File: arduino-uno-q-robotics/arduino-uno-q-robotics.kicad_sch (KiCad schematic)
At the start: 9 parts, among them J1 Conn_02x30_Odd_Even, J2 Conn_02x30_Odd_Even, J3 Connector_FFC-FPC, J4 Connector_FFC-FPC, U1 LSM6DSO32, U2 TCA9803

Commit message: Add STEMMA port to MCU I2C
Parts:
- added U3: ~, Connector_JST:JST_SH_SM04B-SRSS-TB_1x04-1MP_P1.00mm_Horizontal, symbol robotics-symbols:STEMMA
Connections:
- net +3.3V: now also U3.3 (3.3V)
- net GND: now also U3.4 (GND)
- net MCU_I2C4_SCL: now also U3.1 (SCL)
- net MCU_I2C4_SDA: now also U3.2 (SDA)

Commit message: Adjust STEMMA port pin numbers
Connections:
- net +3.3V: now also U3.2 (3.3V); no longer U3.3 (3.3V)
- net GND: now also U3.1 (GND); no longer U3.4 (GND)
- net MCU_I2C4_SCL: now also U3.4 (SCL); no longer U3.1 (SCL)
- net MCU_I2C4_SDA: now also U3.3 (SDA); no longer U3.2 (SDA)

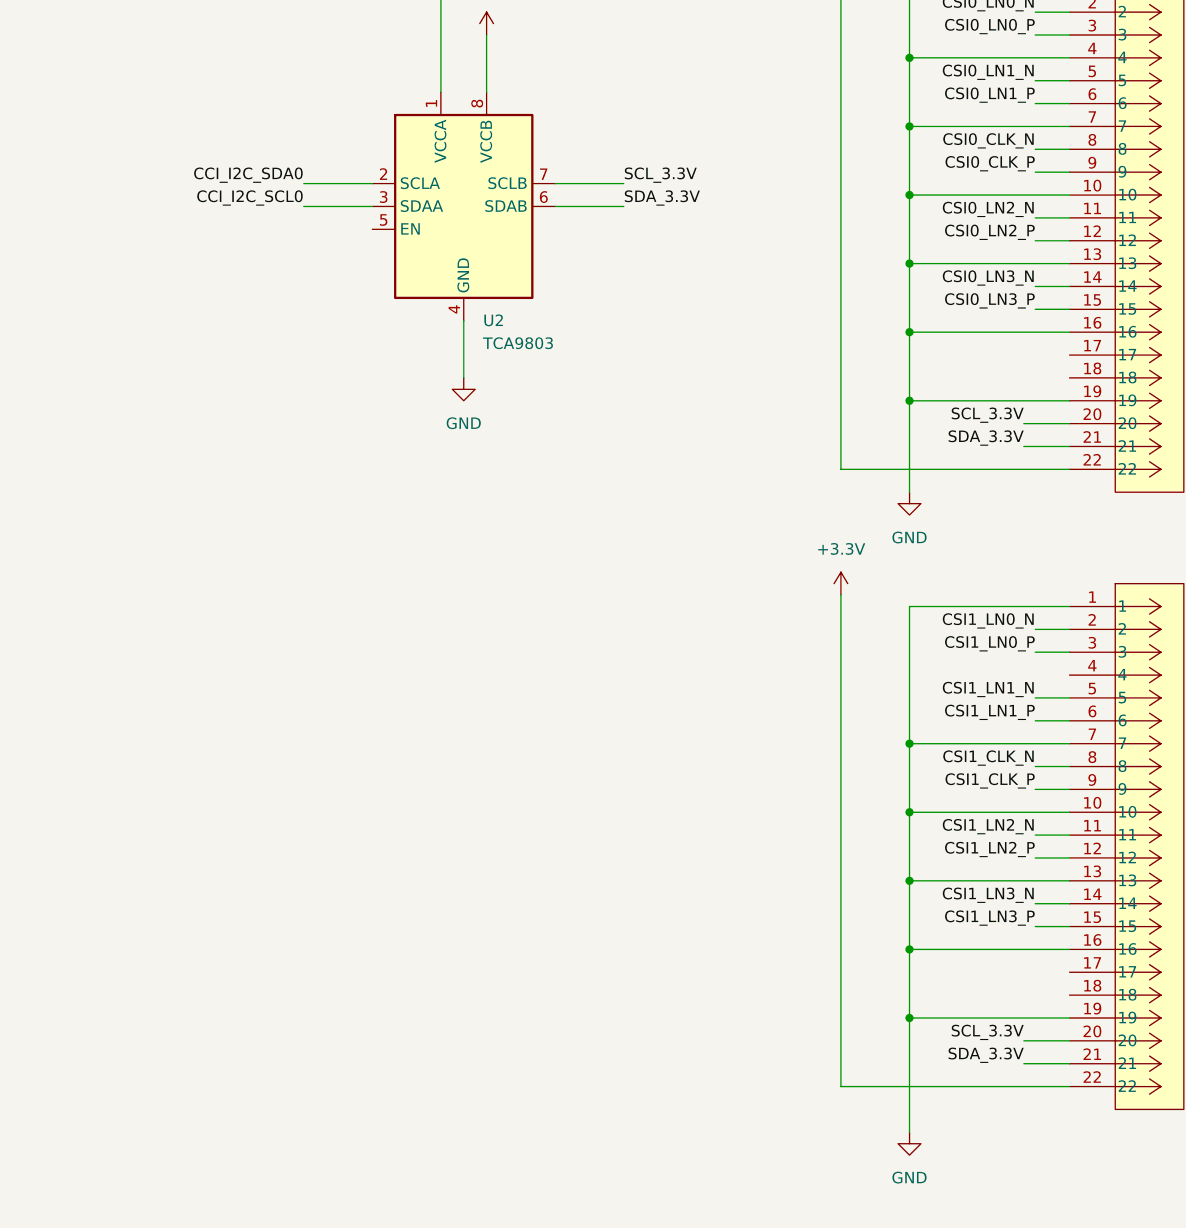
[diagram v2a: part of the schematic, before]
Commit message: Separate camera connectors level shifter
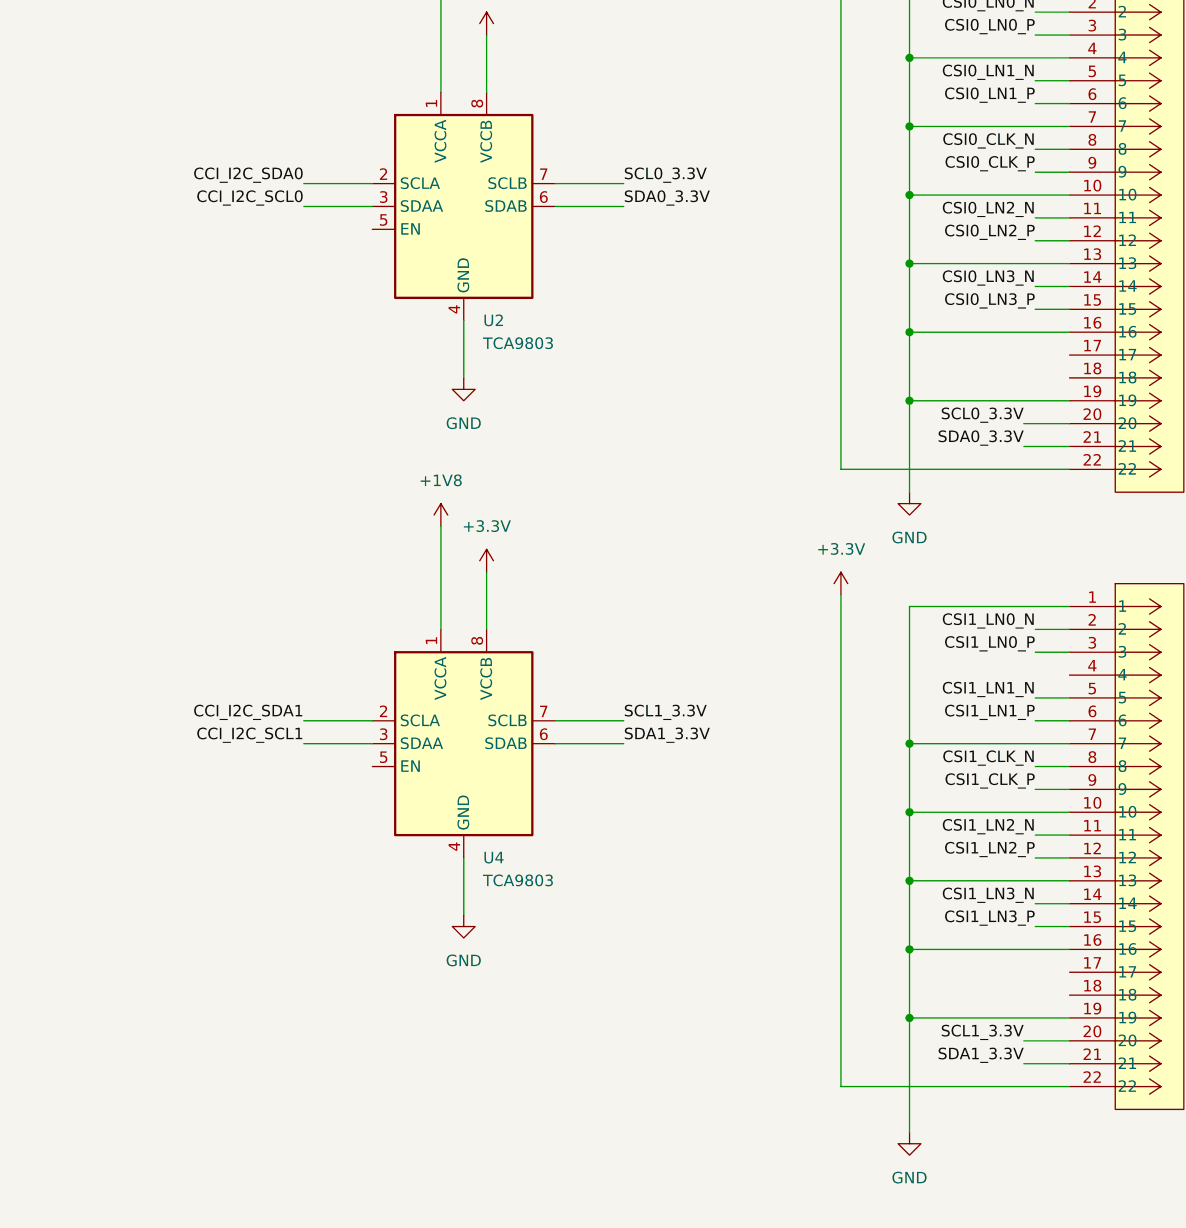
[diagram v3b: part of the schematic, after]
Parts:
- added U4: TCA9803, Package_SO:VSSOP-8_3x3mm_P0.65mm, symbol Interface:TCA9803
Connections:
- net +1V8: now also U4.1 (VCCA)
- net +3.3V: now also U4.8 (VCCB)
- net CCI_I2C_SCL1: now also U4.3 (SDAA)
- net CCI_I2C_SDA1: now also U4.2 (SCLA)
- net GND: now also U4.4 (GND)
- net SCL_3.3V renamed SCL0_3.3V
- net SCL0_3.3V: no longer J4.20
- net SDA_3.3V renamed SDA0_3.3V
- net SDA0_3.3V: no longer J4.21
- new net SCL1_3.3V: J4.20, U4.7 (SCLB)
- new net SDA1_3.3V: J4.21, U4.6 (SDAB)

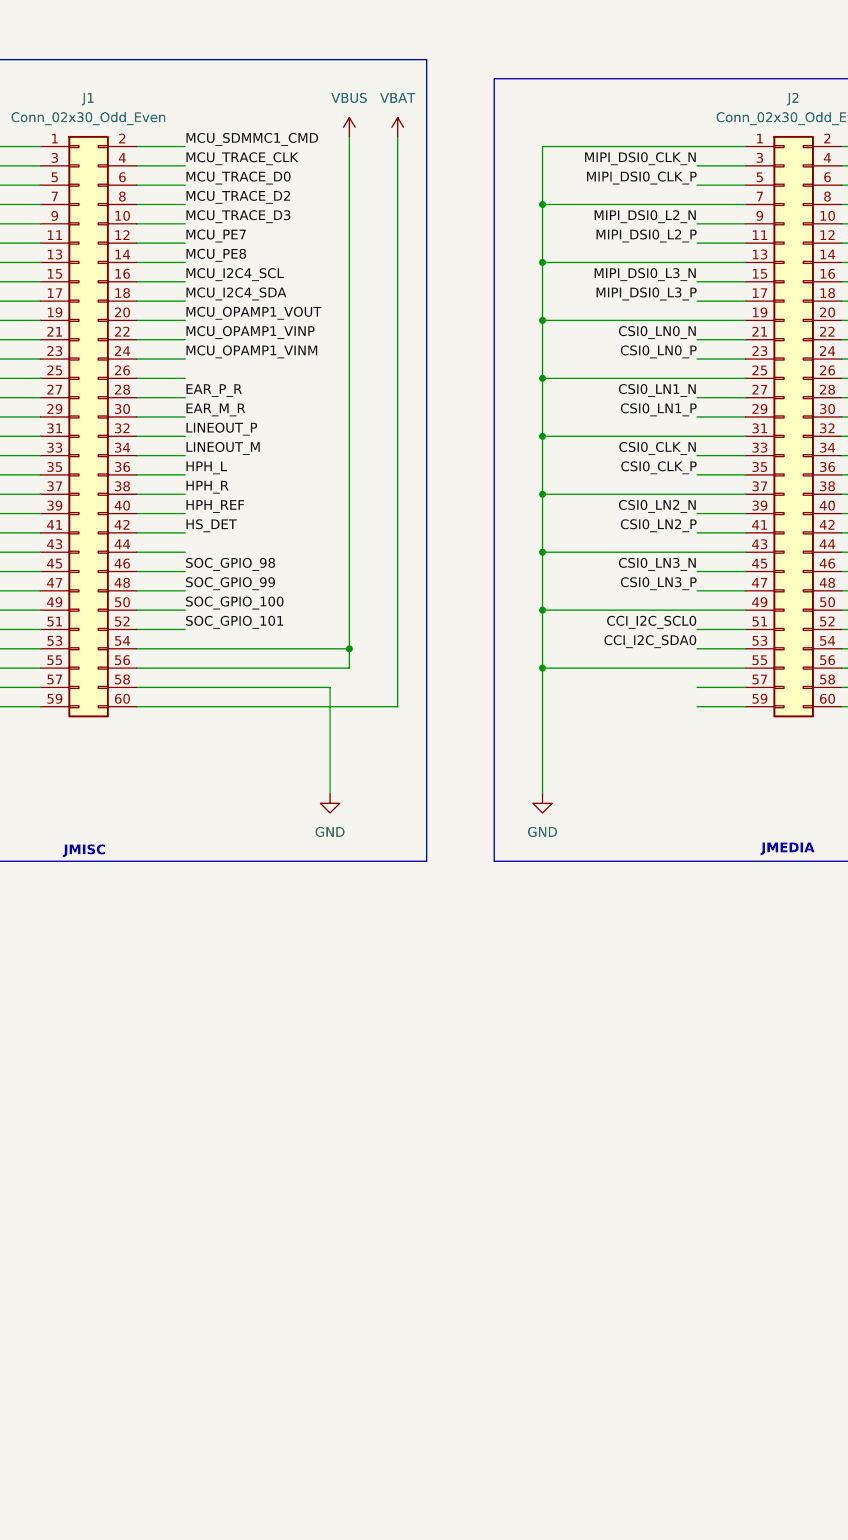
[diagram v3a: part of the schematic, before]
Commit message: Add Pin sockets and headers for JMISC pins
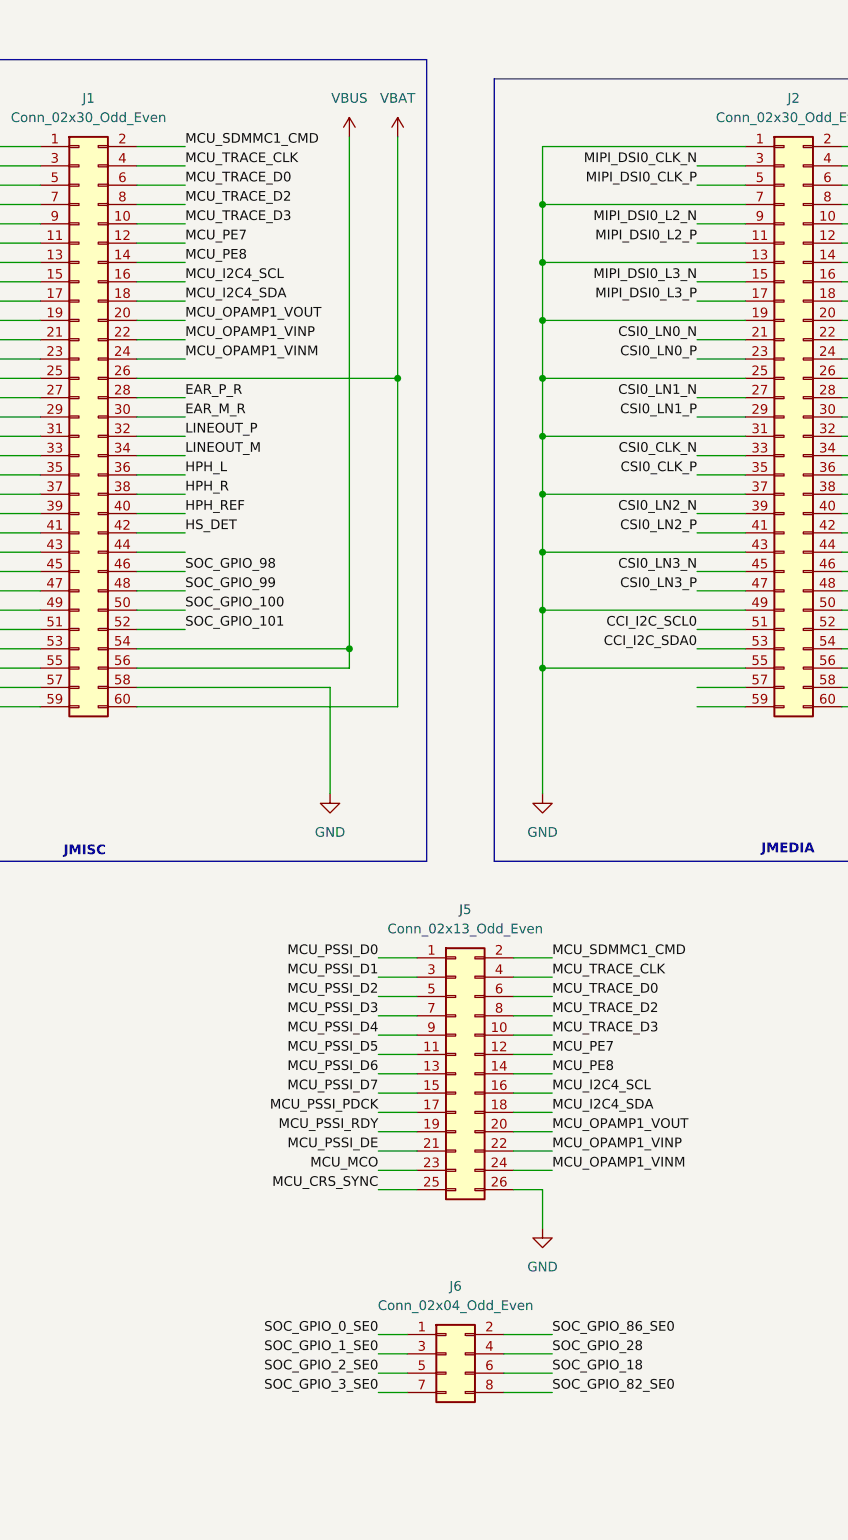
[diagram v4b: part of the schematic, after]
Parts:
- added J5: Conn_02x13_Odd_Even, Connector_PinSocket_2.54mm:PinSocket_2x13_P2.54mm_Vertical_SMD, symbol Connector_Generic:Conn_02x13_Odd_Even
- added J6: Conn_02x04_Odd_Even, Connector_PinHeader_2.54mm:PinHeader_2x04_P2.54mm_Vertical_SMD, symbol Connector_Generic:Conn_02x04_Odd_Even
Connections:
- net GND: now also J5.26 (Pin_26)
- net MCU_CRS_SYNC: now also J5.25 (Pin_25)
- net MCU_I2C4_SCL: now also J5.16 (Pin_16)
- net MCU_I2C4_SDA: now also J5.18 (Pin_18)
- net MCU_MCO: now also J5.23 (Pin_23)
- net MCU_OPAMP1_VINM: now also J5.24 (Pin_24)
- net MCU_OPAMP1_VINP: now also J5.22 (Pin_22)
- net MCU_OPAMP1_VOUT: now also J5.20 (Pin_20)
- net MCU_PE7: now also J5.12 (Pin_12)
- net MCU_PE8: now also J5.14 (Pin_14)
- net MCU_PSSI_D0: now also J5.1 (Pin_1)
- net MCU_PSSI_D1: now also J5.3 (Pin_3)
- net MCU_PSSI_D2: now also J5.5 (Pin_5)
- net MCU_PSSI_D3: now also J5.7 (Pin_7)
- net MCU_PSSI_D4: now also J5.9 (Pin_9)
- net MCU_PSSI_D5: now also J5.11 (Pin_11)
- net MCU_PSSI_D6: now also J5.13 (Pin_13)
- net MCU_PSSI_D7: now also J5.15 (Pin_15)
- net MCU_PSSI_DE: now also J5.21 (Pin_21)
- net MCU_PSSI_PDCK: now also J5.17 (Pin_17)
- net MCU_PSSI_RDY: now also J5.19 (Pin_19)
- net MCU_SDMMC1_CMD: now also J5.2 (Pin_2)
- net MCU_TRACE_CLK: now also J5.4 (Pin_4)
- net MCU_TRACE_D0: now also J5.6 (Pin_6)
- net MCU_TRACE_D2: now also J5.8 (Pin_8)
- net MCU_TRACE_D3: now also J5.10 (Pin_10)
- net SOC_GPIO_0_SE0: now also J6.1 (Pin_1)
- net SOC_GPIO_18: now also J6.6 (Pin_6)
- net SOC_GPIO_1_SE0: now also J6.3 (Pin_3)
- net SOC_GPIO_28: now also J6.4 (Pin_4)
- net SOC_GPIO_2_SE0: now also J6.5 (Pin_5)
- net SOC_GPIO_3_SE0: now also J6.7 (Pin_7)
- net SOC_GPIO_82_SE0: now also J6.8 (Pin_8)
- net SOC_GPIO_86_SE0: now also J6.2 (Pin_2)
- net VBAT: now also J1.26 (Pin_26)

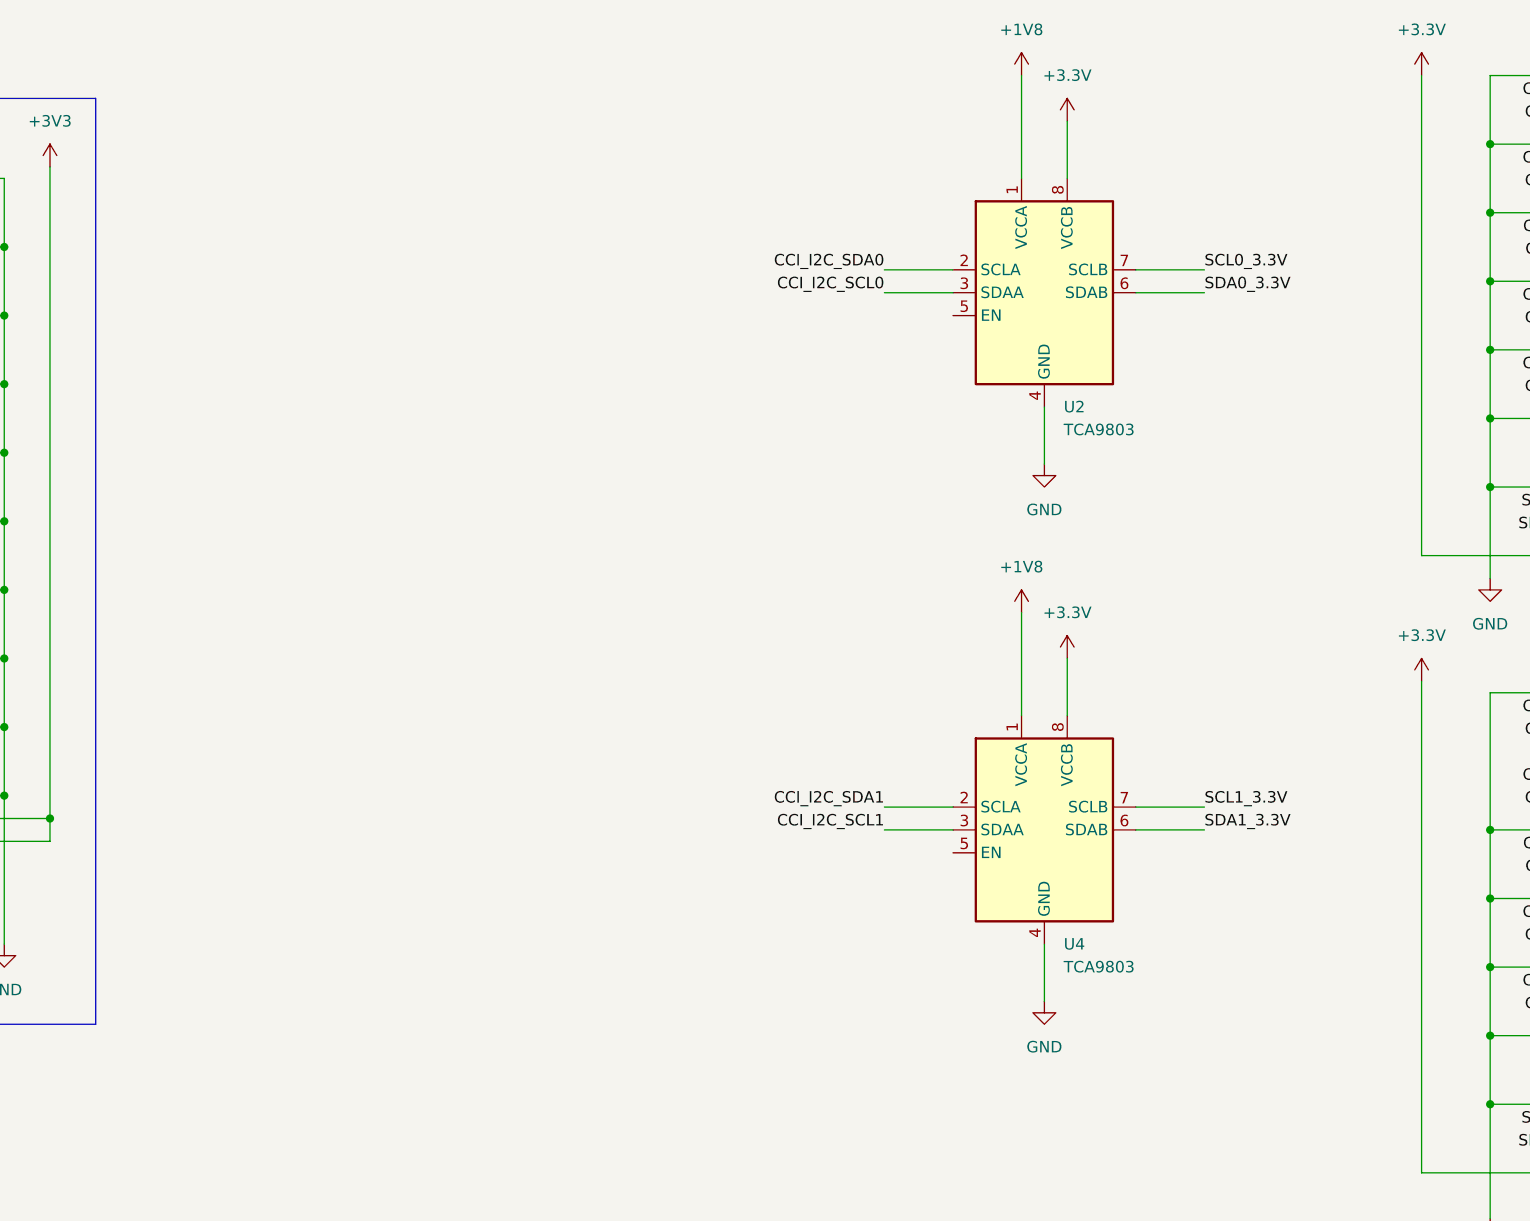
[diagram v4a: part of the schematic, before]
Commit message: Add GPIO voltage steppers to schematic
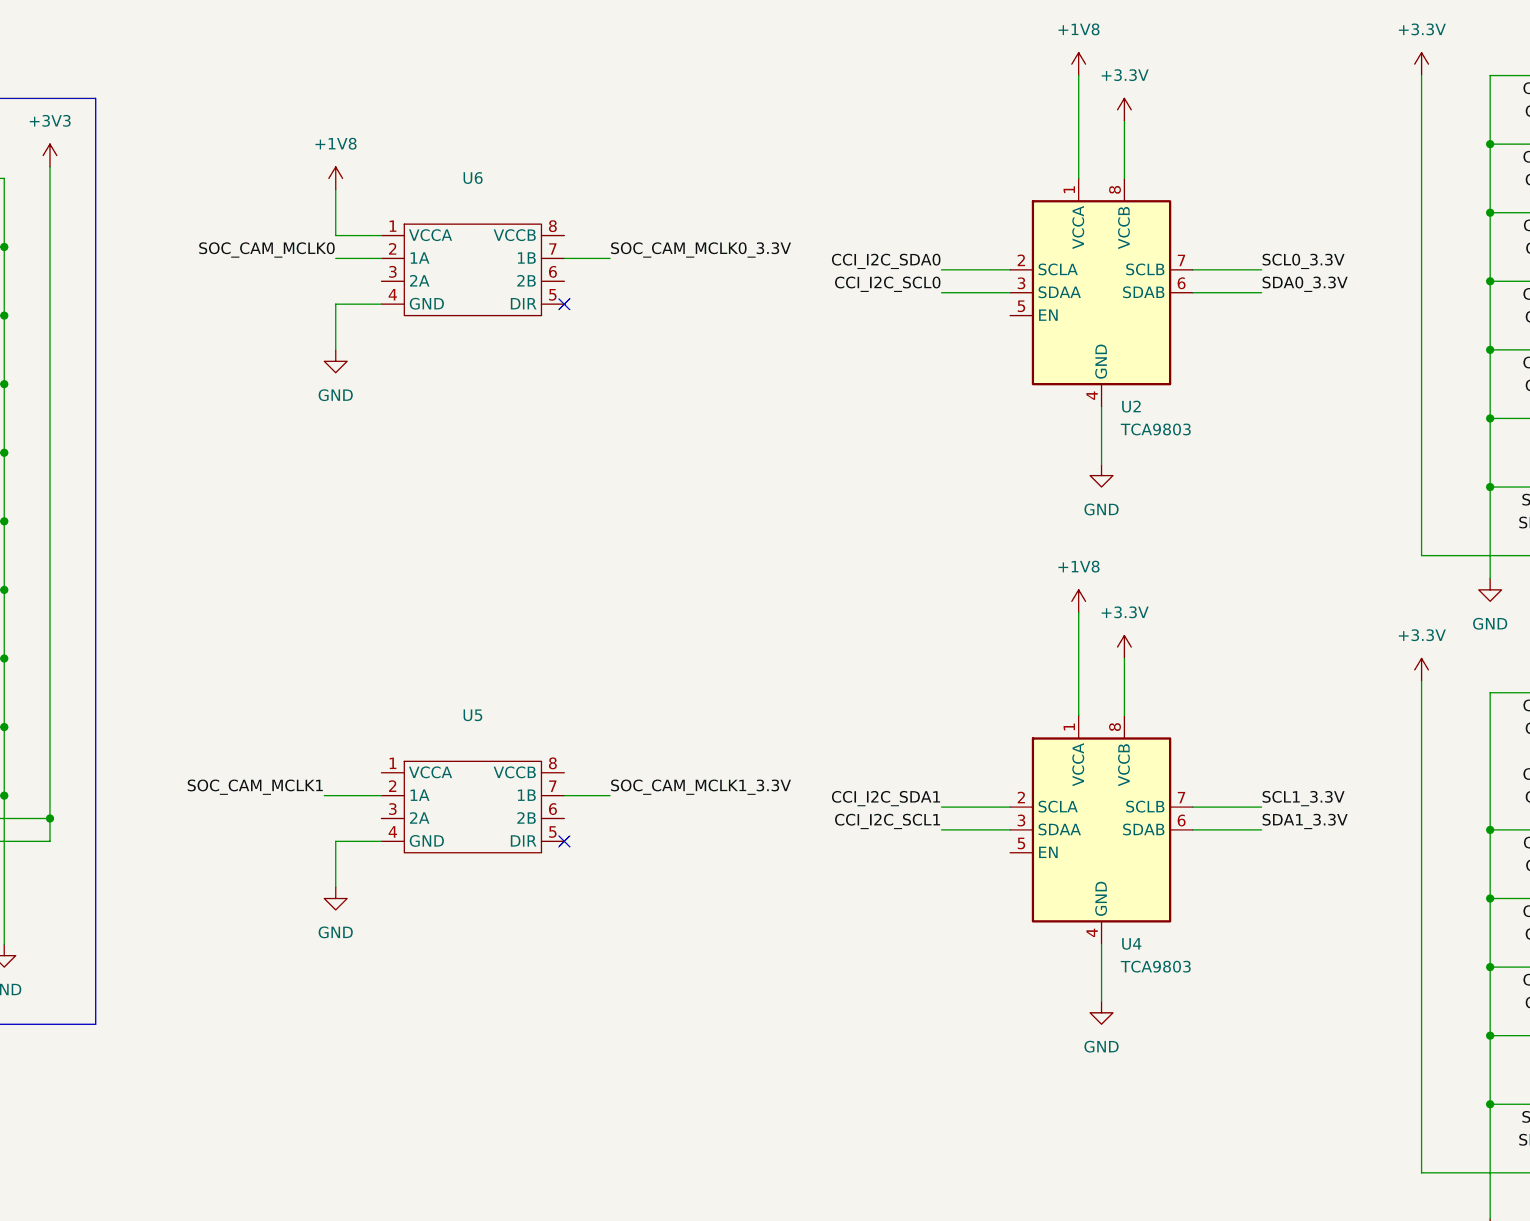
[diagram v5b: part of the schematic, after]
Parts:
- added U5, U6: ~, robotics-footprints:74LVC2T45GS115, symbol robotics-symbols:74LVC2T45GS
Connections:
- net +1V8: now also U6.1 (VCCA)
- net GND: now also U5.4 (GND), U6.4 (GND)
- net SOC_CAM_MCLK0: now also U6.2 (1A)
- net SOC_CAM_MCLK1: now also U5.2 (1A)
- new net SOC_CAM_MCLK0_3.3V: U6.7 (1B)
- new net SOC_CAM_MCLK1_3.3V: U5.7 (1B)
- no-connect marks 5 -> 7
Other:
- moved on the sheet: U2, U4
